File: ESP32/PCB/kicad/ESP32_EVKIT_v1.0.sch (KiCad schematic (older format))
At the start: 45 parts, among them IC1 AP7370Y, IC2 SN65HVD230, J1 O3, M1 ESP32_EVKIT_V1, SW1 ITS-1105-8, SW2 ITS-1105-8, X1 MICRO_SD_ATOM-A01482

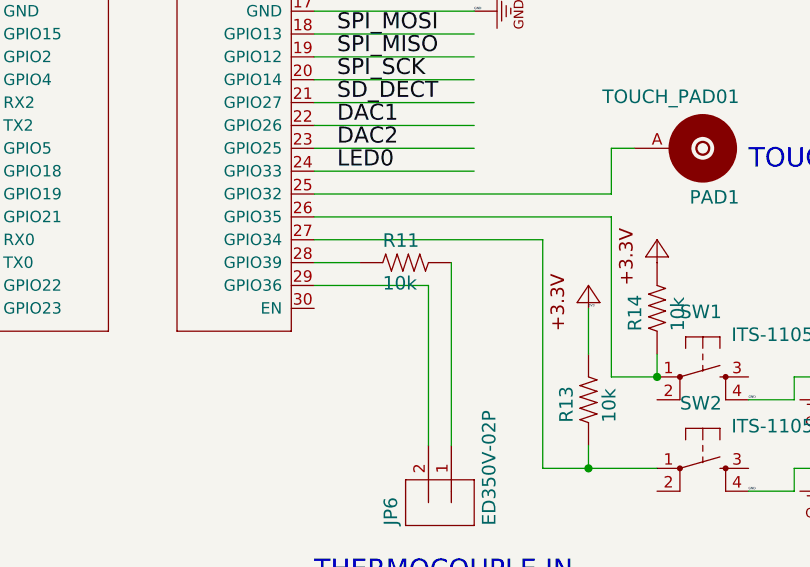
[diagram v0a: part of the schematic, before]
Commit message: ARDUINO 예제 자료 업로드
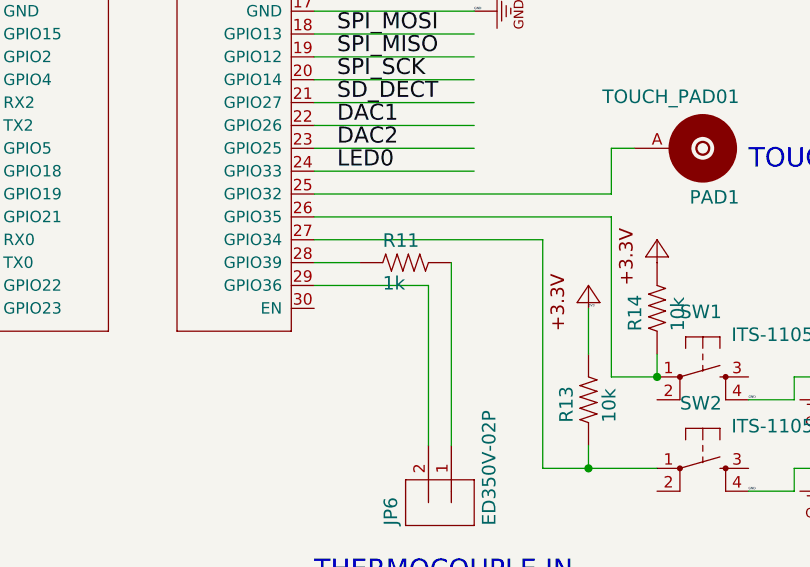
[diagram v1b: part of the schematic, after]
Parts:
- R11: value 10k -> 1k
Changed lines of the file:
@@
 P 8100 3800
 F 0 "R11" H 8000 3862 59  0000 L BNN
-F 1 "10k" H 8000 3675 59  0000 L BNN
+F 1 "1k" H 8000 3675 59  0000 L BNN
 F 2 "ESP32_EVKIT_v1.0:R0603" H 8100 3800 50  0001 C CNN
 F 3 "" H 8100 3800 50  0001 C CNN
